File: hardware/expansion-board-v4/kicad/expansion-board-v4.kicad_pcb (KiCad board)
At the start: 6 copper layers, 100 x 62 mm, 174 parts, among them J1 PinHeader_2x20_P2.54mm_Vertic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, J2 U.FL_Hirose_U.FL-R-SMT-1_Vert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, J4 USB_C_Receptacle_HRO_TYPE-C-3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, J5 U.FL_Hirose_U.FL-R-SMT-1_Vert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, J6 U.FL_Hirose_U.FL-R-SMT-1_Vert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, J7 U.FL_Hirose_U.FL-R-SMT-1_Vert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, J8 U.FL_Hirose_U.FL-R-SMT-1_Vert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, J9 MX1.25WT-2P, Q2 SOT-23, Q3 SOT-23, Q4 SOT-23, Q5 SOT-23, SW2 SolderJumper-2_P1.3mm_Open_Pa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, U1 SOT-23-5, U10 QFN-48-1EP_7x7mm_P0.5mm_EP5.1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, U11 DFN-8-1EP_2x2mm_P0.5mm_EP0.86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, U12 SOT-363_SC-70-6, U14 MSOP-8_3x3mm_P0.65mm, U15 SOT-23-6, U16 SOT-363_SC-70-6, U17 SOT-363_SC-70-6, U18 SOIC-10_3.9x4.9mm_P1mm, U19 QFN-24-1EP_4x4mm_P0.5mm_EP2.6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, U2 SOT-23-5, U20 TSOT-23-6, U3 SOT-23-5, U4 BNO085_LGA-28, U5 BMP388_LGA-10, U6 LGA-16_3x3mm_P0.5mm, U7 ATGM336H_LCC-18, U8 QFN-56-1EP_7x7mm_P0.4mm_EP3.2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, U9 SOIC-8_5.3x5.3mm_P1.27mm, Y1 Crystal_SMD_3225-4Pin_3.2x2.5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, Y2 Crystal_SMD_3225-4Pin_3.2x2.5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, Y3 Crystal_SMD_3215-2Pin_3.2x1.5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

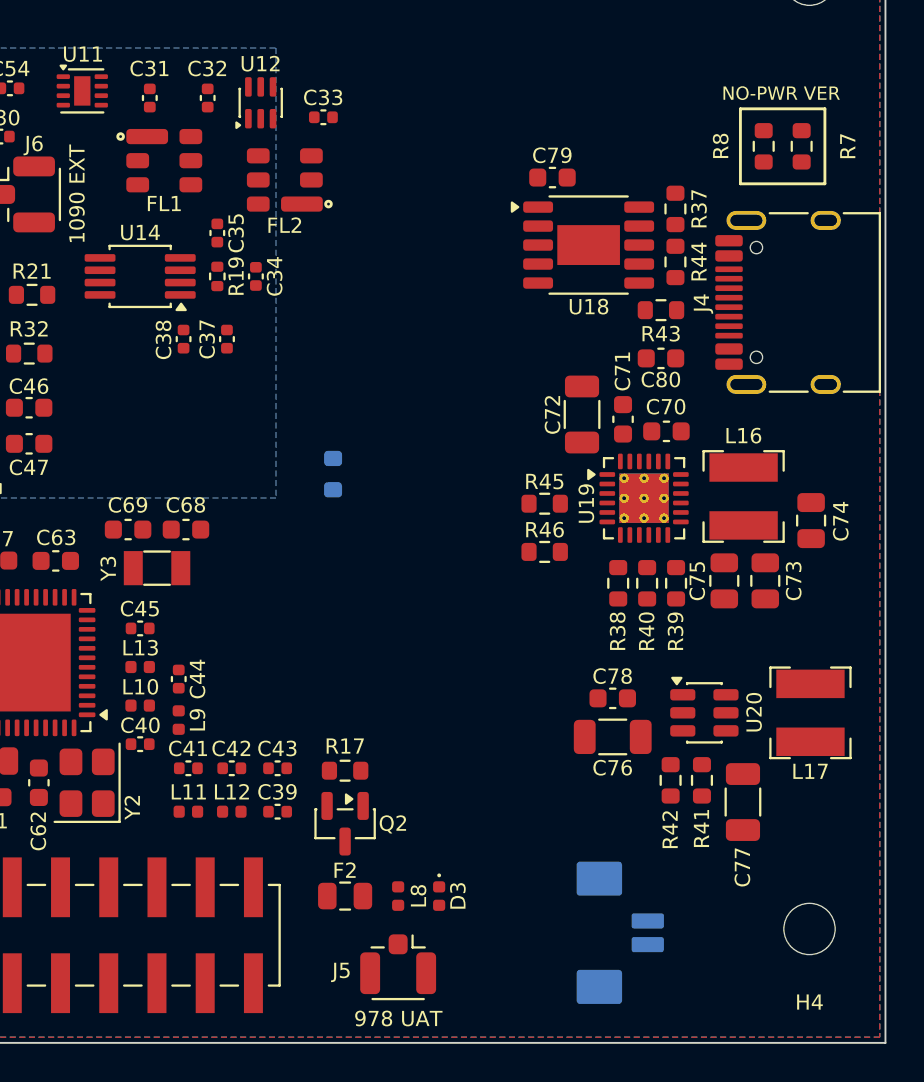
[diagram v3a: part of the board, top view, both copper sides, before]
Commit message: chore(v4): 固化布线前的最终布局（978 重排 + 电源回路全绿）
978 链：ANT_978 节点 14.50 → 5.56mm（L11/L12/C39 竖排北上直接进 L8/J5，
消掉上一版 C39→L8 那 10mm 空档）；节点合计 46.96 → 41.07mm。
主路径 U10.RF_P→L9→L11→L12→C39→L8→J5 全程单调。
对地支路 C41/C42/C43 均 2.29mm、C44 2.40、C45 2.03；D3(ESD)→J5 1.63mm。

电源三级功率回路全部达标（用户本轮修好了我先前标的三处）：
  C70 1.59 / C71 1.68 / R37 1.94 / R38 2.36 / C77 2.44 / C72 2.99
  L16 4.00 / R41 3.82 / L17 4.70mm
courtyard 重叠归零（C72↔U19、R37↔R44 已解）。

DRC 8 条 0 error、未连接 284、parity 0。
下一步跑 run_route.sh。备份 /tmp/pcb_before_route.kicad_pcb
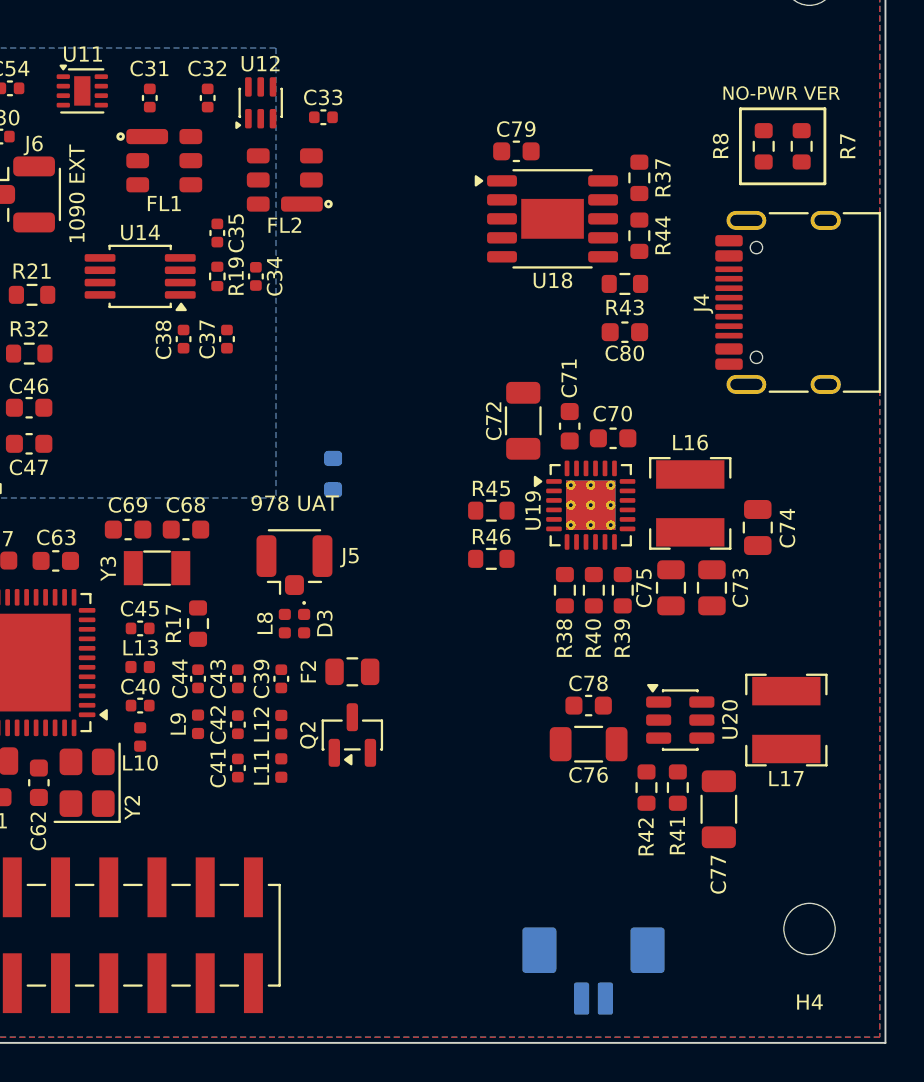
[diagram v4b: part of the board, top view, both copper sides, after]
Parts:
- moved J5 22.6 mm to (118.9, 86.4), turned to 90 degrees
- moved D3 16.0 mm to (119.4, 89.9)
- moved L8 15.5 mm to (118.4, 89.9), turned to 90 degrees
- moved F2 11.8 mm to (121.9, 92.5), turned to 180 degrees
- moved R17 11.0 mm to (113.8, 89.9), turned to 90 degrees
- moved C39 7.00 mm to (118.2, 92.8), turned to 90 degrees
- moved L11 5.41 mm to (118.2, 97.5), turned to 90 degrees
- moved L12 5.27 mm to (118.2, 95.2), turned to 90 degrees
- moved C43 5.15 mm to (115.9, 92.8), turned to 90 degrees
- moved Q2 4.69 mm to (121.9, 95.8), turned to 90 degrees
- moved J9 4.49 mm to (134.6, 109.7), turned to 0 degrees
- moved C72 3.11 mm to (130.9, 79.2)
- moved C70 2.83 mm to (135.7, 80.2)
- moved C71 2.83 mm to (133.4, 79.5)
- moved C73 2.83 mm to (140.9, 88.0)
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
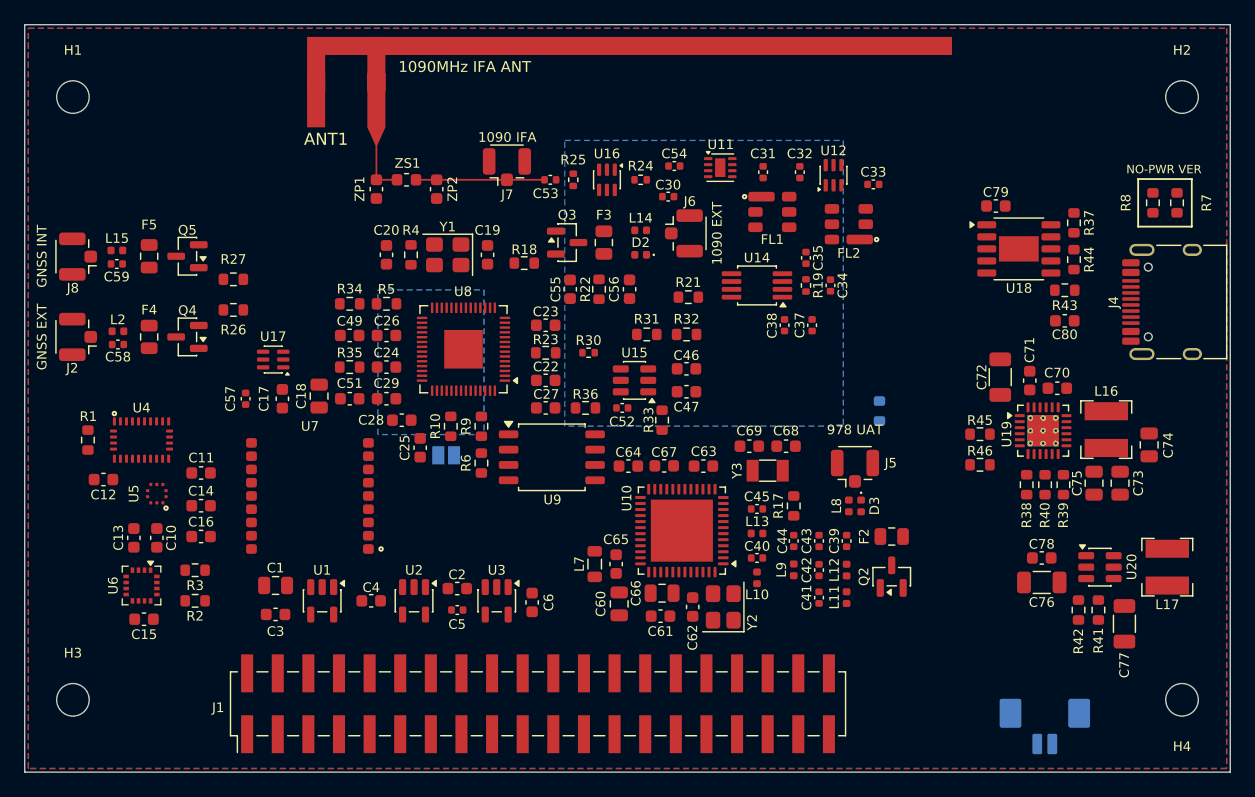
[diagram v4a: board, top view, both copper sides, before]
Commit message: chore(v4): 固化 2026-08-28 这一版——DRC 零违例、未连通 0
板子状态：
    DRC        {} 一条不剩（含 text_height）
    未连通     0
    In1 走线   0        射频 103 段全 F.Cu    射频过孔 0
    元件重叠   0        焊盘重叠 0            丝印重叠 0

固化四件套：
    PLACEMENT.py  174 元件 + 174 位号（位置/朝向/面/位号坐标）
    SILK.json     16 条板级文字 + 4 个丝印图形
    ROUTES.json   1356 段走线 + 382 过孔
    ZONES.json    15 个覆铜区

BAT_P 干路由罩哥手工重走：原来 79% 的长度（22.67mm）在 In2 信号层 0.15mm，
内层 0.5oz 铜载流只有外层一半（0.29A@ΔT10），对 2A 过载 7 倍。现改为全程
F.Cu 0.5mm 绕西侧通道，J9 端 4 个并联过孔（7.61A）。

.kicad_pro 的网络类模式随之更新：BAT_P/SYS_4V/CHG_PMID → POWER，
CHG_LX/BST_LX/SUBG_SW → POWER_LO。
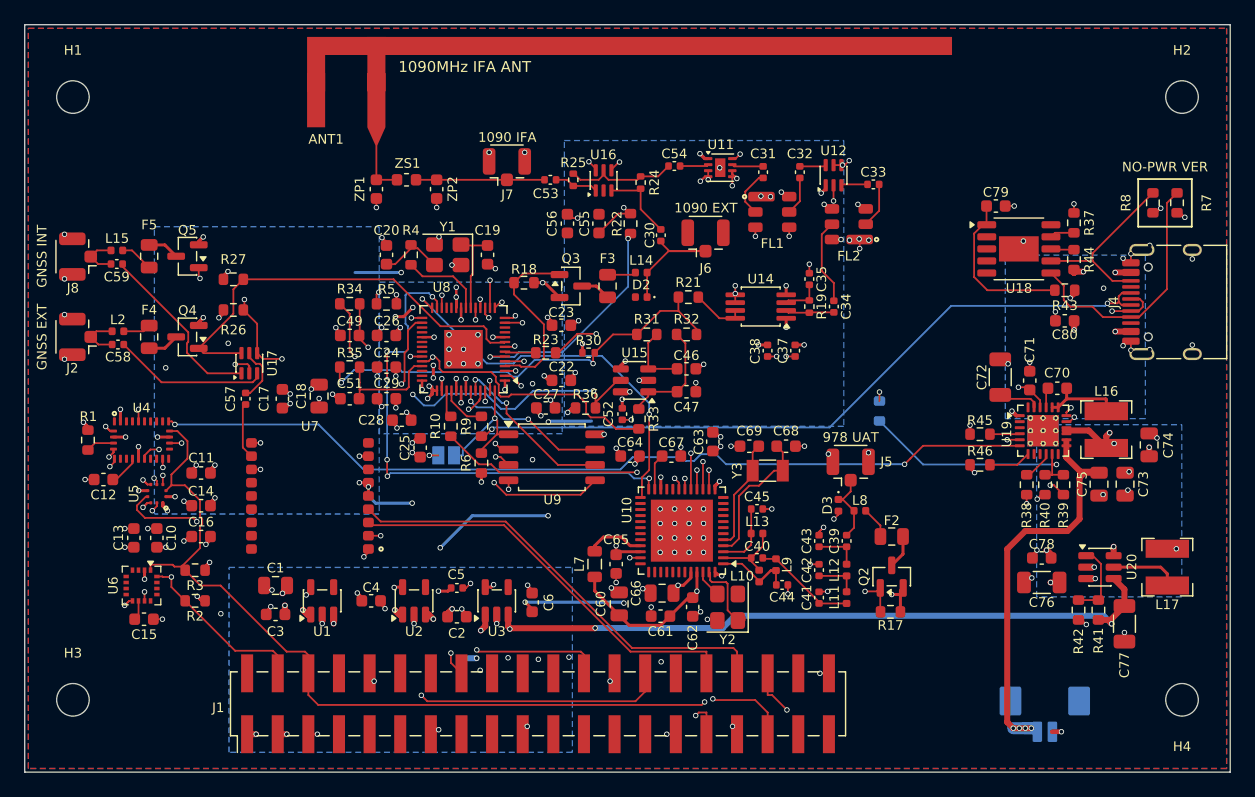
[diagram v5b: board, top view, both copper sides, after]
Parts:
- C72: value C_0603_1608Metric -> C_1206_3216Metric
- C73, C74, C75: value C_0603_1608Metric -> C_0805_2012Metric
- R7, R8: value 5.1k -> R_0603_1608Metric
- RT1: value NCP18XH103F03RB 10k NTC -> R_0603_1608Metric
- moved R17 11.9 mm to (121.8, 98.7), turned to 180 degrees
- moved C56 7.50 mm to (95.0, 66.5)
- moved R22 6.04 mm to (100.3, 66.5)
- moved C55 5.95 mm to (97.6, 66.5)
- moved C44 3.77 mm to (112.8, 96.5), turned to 0 degrees
- moved F3 3.62 mm to (98.3, 71.7)
- moved Q3 3.62 mm to (95.3, 71.7)
- moved D2 3.51 mm to (101.1, 72.6)
- moved L14 3.51 mm to (101.1, 70.6)
- moved C30 3.26 mm to (102.8, 67.5), turned to 90 degrees
- moved C37 2.54 mm to (113.9, 77.0)
- moved C38 2.54 mm to (111.6, 77.0)
- moved C2 2.34 mm to (85.9, 99.1)
- moved C63 2.17 mm to (107.1, 84.6), turned to 90 degrees
- moved U17 2.00 mm to (68.6, 78.1), turned to 90 degrees
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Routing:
- net GND: track 0.00 -> 139.5 mm, vias 0 -> 179
- net I2C_SCL: track 0.00 -> 107.1 mm, vias 0 -> 2
- net I2C_SDA: track 0.00 -> 103.4 mm, vias 0 -> 4
- net 3V3_GNSS: track 0.00 -> 81.0 mm, vias 0 -> 16
- net VCC_5V: track 0.00 -> 72.3 mm, vias 0 -> 14
- net USB_DM: track 0.00 -> 67.2 mm, vias 0 -> 2
- net USB_DP: track 0.00 -> 60.2 mm, vias 0 -> 2
- net IMU_INT: track 0.00 -> 52.1 mm, vias 0 -> 2
- net 3V3_DIG: track 0.00 -> 51.0 mm, vias 0 -> 45
- net BARO_INT: track 0.00 -> 45.7 mm, vias 0 -> 2
- net ADSB_TXD: track 0.00 -> 45.5 mm, vias 0 -> 2
- net GNSS_TXD: track 0.00 -> 45.4 mm, vias 0 -> 2
- net SUBG_TMSC: track 0.00 -> 43.2 mm, vias 0 -> 6
- net BIAS_EN_978: track 0.00 -> 41.8 mm, vias 0 -> 2
- net 3V3_RF: track 0.00 -> 39.6 mm, vias 0 -> 15
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- added copper zone on B.Cu, net 3V3_GNSS
- added copper zone on B.Cu, net SYS_4V
- added copper zone on B.Cu, net USB_VBUS
- added copper zone on B.Cu, net VCC_5V

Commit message: chore(v4): 固化——DRC 零违例，且脚本可 1:1 复现
从 PLACEMENT.py / ROUTES.json / SILK.json / ZONES.json 走完整重建链
（gen_pcb → import_routes → route_ifa_feed → silk_texts → silk_size →
gen_polarity_marks），与手上这块板逐维度比对：

    元件       174 / 174    ✅
    位号       174 / 174    ✅
    封装丝印   174 / 174    ✅
    走线      1249 /1249    ✅（仅 50nm 取整）
    过孔       389 / 389    ✅（仅  1nm 取整）
    覆铜区      15 /  15    ✅
    板级丝印    26 /  26    ✅
    未连通       0 /   0    ✅

BAT_P 干路已由罩哥手工重走完毕：全程 F.Cu ≥0.5mm，J9 端 4 个并联过孔。
CHG_PMID 在 U19 引脚区维持 0.15mm——实测那 2.2mm 段夹在 C71.1 与
U19.24[空脚 DSEL] 之间，几何上限只有 0.10mm，0.25 放不下。
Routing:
- net GND: vias 179 -> 186
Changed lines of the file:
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@@
 		(attr smd)
 		(duplicate_pad_numbers_are_jumpers no)
-		(fp_circle
-			(center -1.09 0)
-			(end -1.04 0)
-			(stroke
-				(width 0.1)
-				(type solid)
-			)
-			(fill no)
-			(layer "F.SilkS")
-		)
 		(fp_rect
 			(start -0.93 -0.47)
@@
 		(attr smd)
 		(duplicate_pad_numbers_are_jumpers no)
-		(fp_circle
-			(center -1.09 0)
-			(end -1.04 0)
-			(stroke
-				(width 0.1)
-				(type solid)
-			)
-			(fill no)
-			(layer "F.SilkS")
-		)
 		(fp_rect
 			(start -0.93 -0.47)
@@
 	)
 	(gr_line
+		(start 102.233 72.243)
+		(end 102.233 72.943)
+		(stroke
+			(width 0.2)
+			(type default)
+		)
+		(layer "F.SilkS")
+	)
+	(gr_line
+		(start 117.15 88.775)
+		(end 117.85 88.775)
+		(stroke
+			(width 0.2)
+			(type default)
+		)
+		(layer "F.SilkS")
+	)
+	(gr_line
 		(start 142.362 62.801)
 		(end 146.812 62.801)
@@
 	)
 	(via
-		(at 132.84 67.9465)
+		(at 64.23 86.5355)
 		(size 0.45)
 		(drill 0.3)
@@
 	)
 	(via
-		(at 64.23 86.5355)
+		(at 104.422 85.034)
 		(size 0.45)
 		(drill 0.3)
@@
 	)
 	(via
-		(at 104.422 85.034)
+		(at 107.651 61.868)
 		(size 0.45)
 		(drill 0.3)
@@
 	)
 	(via
-		(at 107.651 61.868)
+		(at 74.28 108.855)
 		(size 0.45)
 		(drill 0.3)
@@
 	)
 	(via
-		(at 74.28 108.855)
+		(at 133.065 69.196)
 		(size 0.45)
 		(drill 0.3)
@@
 	)
 	(via
+		(at 133.065 67.996)
+		(size 0.45)
+		(drill 0.3)
+		(layers "F.Cu" "B.Cu")
+		(net "GND")
+	)
+	(via
 		(at 87.398 74.4825)
 		(size 0.45)
@@
 	)
 	(via
+		(at 133.877999 83.078)
+		(size 0.45)
+		(drill 0.3)
+		(layers "F.Cu" "B.Cu")
+		(net "GND")
+	)
+	(via
 		(at 117.714 67.818)
 		(size 0.45)
@@
 	)
 	(via
+		(at 133.877999 84.278)
+		(size 0.45)
+		(drill 0.3)
+		(layers "F.Cu" "B.Cu")
+		(net "GND")
+	)
+	(via
 		(at 106.696 62.858)
 		(size 0.45)
@@
 	)
 	(via
+		(at 131.865 67.996)
+		(size 0.45)
+		(drill 0.3)
+		(layers "F.Cu" "B.Cu")
+		(net "GND")
+	)
+	(via
 		(at 89.154 99.6775)
 		(size 0.45)
@@
 	)
 	(via
+		(at 135.078 84.278)
+		(size 0.45)
+		(drill 0.3)
+		(layers "F.Cu" "B.Cu")
+		(net "GND")
+	)
+	(via
 		(at 85.44 69.938)
 		(size 0.45)
@@
 	)
 	(via
+		(at 135.078 83.078)
+		(size 0.45)
+		(drill 0.3)
+		(layers "F.Cu" "B.Cu")
+		(net "GND")
+	)
+	(via
 		(at 101.968 98.31)
 		(size 0.45)
@@
 	)
 	(via
+		(at 131.865 69.196)
+		(size 0.45)
+		(drill 0.3)
+		(layers "F.Cu" "B.Cu")
+		(net "GND")
+	)
+	(via
 		(at 110.614 67.552)
 		(size 0.45)
@@
 	(segment
 		(start 132 108.3574)
-		(end 133.5 108.3574)
+		(end 133.65 108.3574)
 		(width 0.5)
 		(layer "F.Cu")
@@
 	)
 	(via
-		(at 133 108.3574)
+		(at 133.1 108.3574)
 		(size 0.45)
 		(drill 0.3)
@@
 	)
 	(via
-		(at 133.5 108.3574)
+		(at 133.65 108.3574)
 		(size 0.45)
 		(drill 0.3)
@@
 	)
 	(via
-		(at 132.5 108.3574)
+		(at 132.55 108.3574)
 		(size 0.45)
 		(drill 0.3)
@@
 	)
 	(segment
-		(start 133.5 108.3574)
+		(start 133.65 108.3574)
 		(end 133.7024 108.3574)
 		(width 0.5)
@@
 	)
 	(segment
-		(start 132.5 108.3574)
-		(end 133 108.3574)
+		(start 132.55 108.3574)
+		(end 133.1 108.3574)
 		(width 0.5)
 		(layer "B.Cu")
@@
 	)
 	(segment
-		(start 133 108.3574)
-		(end 133.5 108.3574)
+		(start 133.1 108.3574)
+		(end 133.65 108.3574)
 		(width 1)
 		(layer "B.Cu")
@@
 		(start 138.054 94.996)
 		(end 138.724 94.996)
-		(width 0.31)
+		(width 0.48)
 		(layer "F.Cu")
 		(net "SYS_4V")
@@
 		(start 111.0718 96.0906)
 		(end 111.8844 95.278)
-		(width 0.2)
+		(width 0.15)
 		(layer "F.Cu")
 		(net "SUBG_RFP")
@@
 		(start 111.8844 95.278)
 		(end 112.319 95.278)
-		(width 0.2)
+		(width 0.15)
 		(layer "F.Cu")
 		(net "SUBG_RFP")
@@
 		(start 110.871 96.0906)
 		(end 111.0718 96.0906)
-		(width 0.2)
+		(width 0.15)
 		(layer "F.Cu")
 		(net "SUBG_RFP")
